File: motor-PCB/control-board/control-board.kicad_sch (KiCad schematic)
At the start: 22 parts, among them J1 Power Input, J2 Motor, J3 Optocoupler, J4 Conn_01x04, J5 Connection with second PCB, U1 LM7812_TO220, U2 INA219BxDCN, U3 LM7805_TO220, U4 TMP117xxDRV

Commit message: Final Control-Board
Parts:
- removed C8: 0.1u, Capacitor_THT:C_Disc_D5.0mm_W2.5mm_P2.50mm, symbol Device:C
- removed J4: Conn_01x04, Custom:1x04_P2.54mm_Horizontal, symbol Connector_Generic:Conn_01x04
- C3: value 0.1u -> 100nF
- C6: value 10u -> 10µF
- C7: value 0.1u -> 0.1µF
- J1, J2: footprint Custom:1x02_P2.54mm_Horizontal -> TerminalBlock_CUI:TerminalBlock_CUI_TB007-508-02_1x02_P5.08mm_Horizontal
- R1: footprint Resistor_THT:R_Axial_DIN0414_L11.9mm_D4.5mm_P15.24mm_Horizontal -> Resistor_THT:R_Axial_DIN0414_L11.9mm_D4.5mm_P15.24mm_Horizonta
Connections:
- net D8: now also A1.11 (D8)
- net D3: no longer names the net of A1.6 (D3)
- net D5: no longer names the net of A1.8 (D5)
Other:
- note removed: "Heating pad and Fan Control"
- note removed: "TIMER0"
- note removed: "TIMER2"
- moved on the sheet: A1, J3, J5, R2, R3, U4

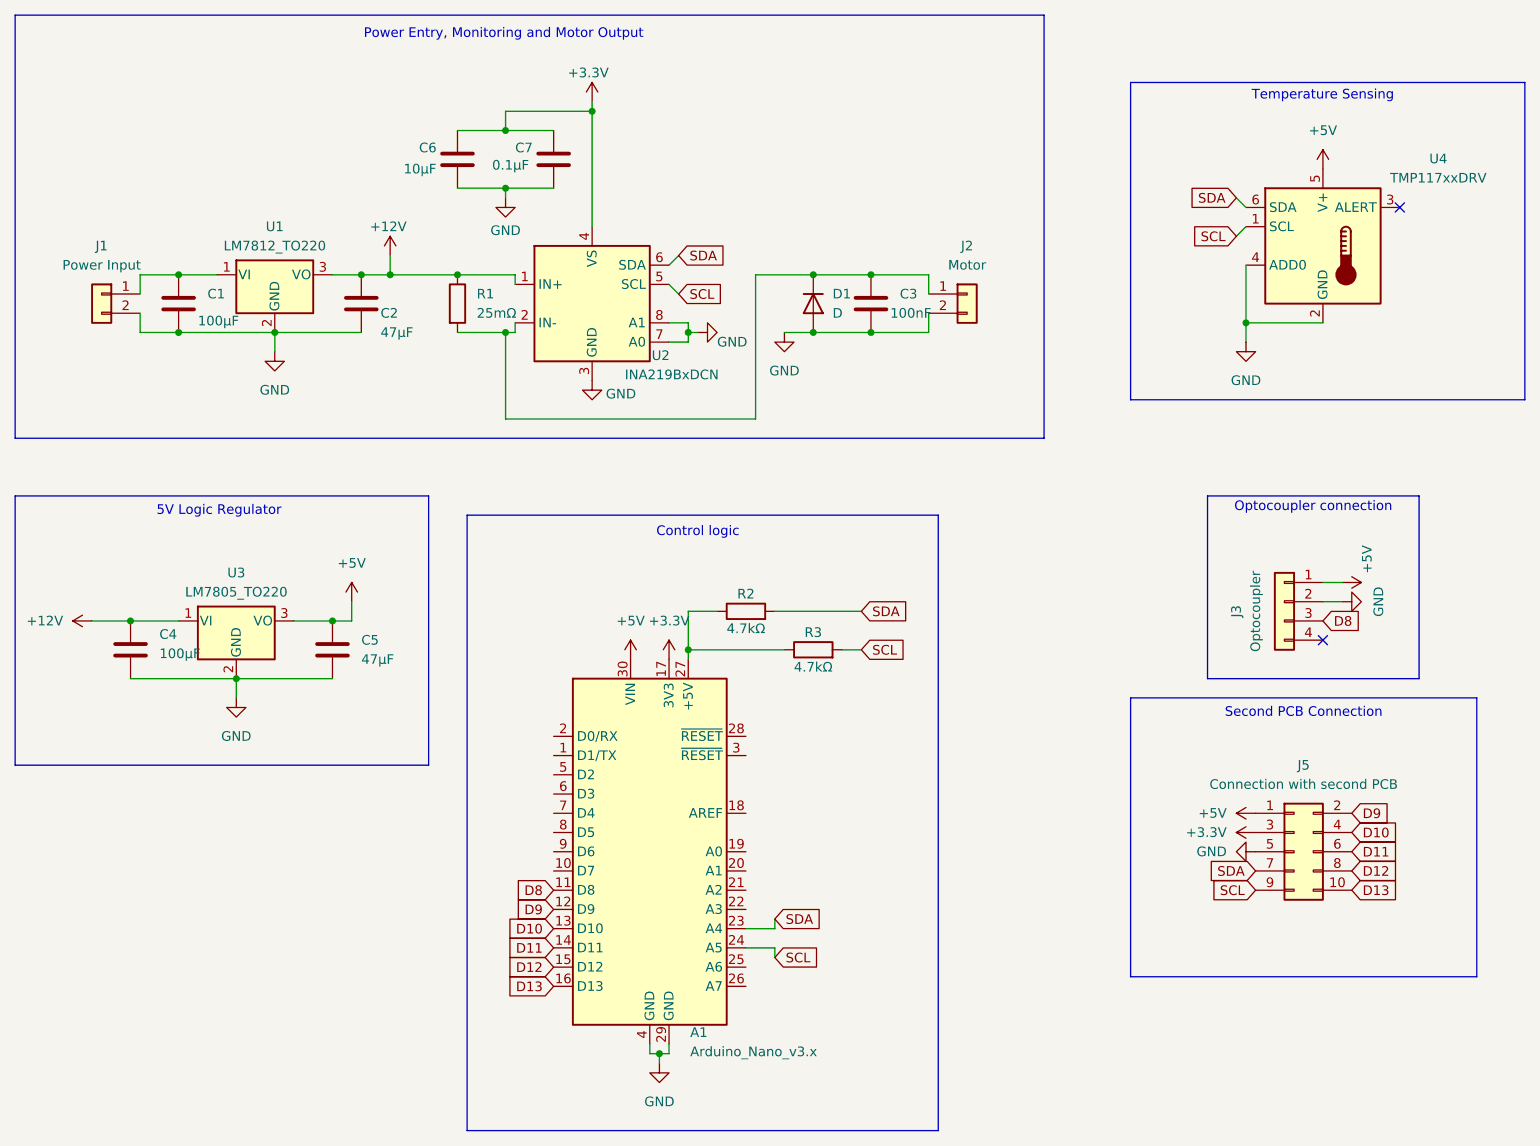
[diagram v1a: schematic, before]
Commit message: added a missing capacitor in the control-board. Added pins to be able to control the heating pad and fan and text. In the generator changed the transistor layout and also added text
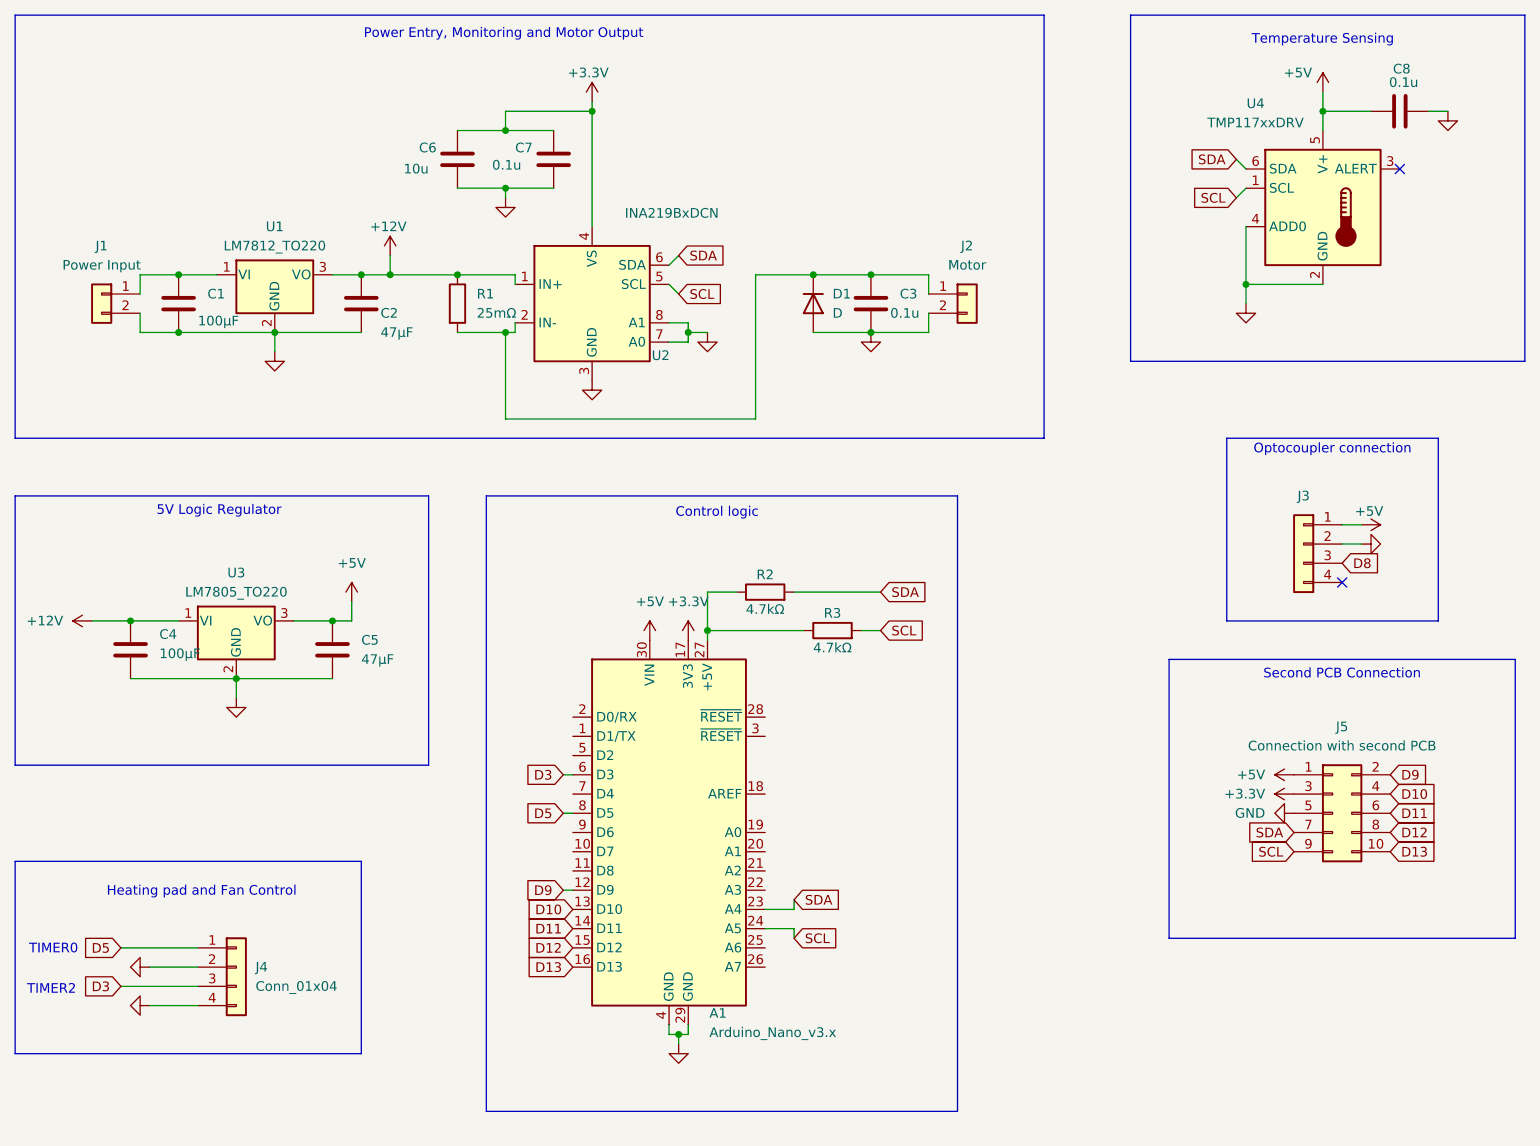
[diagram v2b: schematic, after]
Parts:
- added C8: 0.1u, Capacitor_THT:C_Disc_D5.0mm_W2.5mm_P2.50mm, symbol Device:C
- added J4: Conn_01x04, Custom:1x04_P2.54mm_Horizontal, symbol Connector_Generic:Conn_01x04
- C3: value 100nF -> 0.1u
- C6: value 10µF -> 10u
- C7: value 0.1µF -> 0.1u
- J1, J2: footprint TerminalBlock_CUI:TerminalBlock_CUI_TB007-508-02_1x02_P5.08mm_Horizontal -> Custom:1x02_P2.54mm_Horizontal
- R1: footprint Resistor_THT:R_Axial_DIN0414_L11.9mm_D4.5mm_P15.24mm_Horizonta -> Resistor_THT:R_Axial_DIN0414_L11.9mm_D4.5mm_P15.24mm_Horizontal
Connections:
- net +5V: now also C8.1
- net D8: no longer A1.11 (D8)
- net GND: now also C8.2, J4.2 (Pin_2), J4.4 (Pin_4)
- net D3: now reaches A1.6 (D3)
- net D3: now also J4.3 (Pin_3)
- net D5: now reaches A1.8 (D5)
- net D5: now also J4.1 (Pin_1)
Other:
- note added: "Heating pad and Fan Control"
- note added: "TIMER0"
- note added: "TIMER2"
- moved on the sheet: A1, J3, J5, R2, R3, U4
